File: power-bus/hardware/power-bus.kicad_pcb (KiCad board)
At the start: 2 copper layers, 109.2 x 68.6 mm, 18 parts, among them J1 CONN_01X02, J10 CONN_01X02, J11 CONN_01X02, J12 CONN_01X02, J13 CONN_01X02, J2 CONN_01X02, J3 CONN_01X02, J4 CONN_01X02, J5 CONN_01X02, J6 CONN_01X02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

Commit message: Mounting holes, logos.
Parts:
- added G***: LOGO, conservify:conservify_text_negative_4000, F.Cu at (188.3, 97.3)
- added M1: MOUNT_HOLE, conservify:HOLE_NPTH_3.2MM, F.Cu at (84.8, 52.1)
- added M2: MOUNT_HOLE, conservify:HOLE_NPTH_3.2MM, F.Cu at (169.8, 52.1)
- added M3: MOUNT_HOLE, conservify:HOLE_NPTH_3.2MM, F.Cu at (177.3, 115.1)
- moved J9 5.72 mm to (100.1, 52.1)
- moved J1 1.29 mm to (181.6, 54.5)
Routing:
- net /VADJ_1_EN: track 12.0 -> 16.0 mm
- net /12V0_2_EN: track 27.7 -> 29.5 mm
- net /12V0_1_EN: track 48.1 -> 49.8 mm
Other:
- board text added: "v0.1"

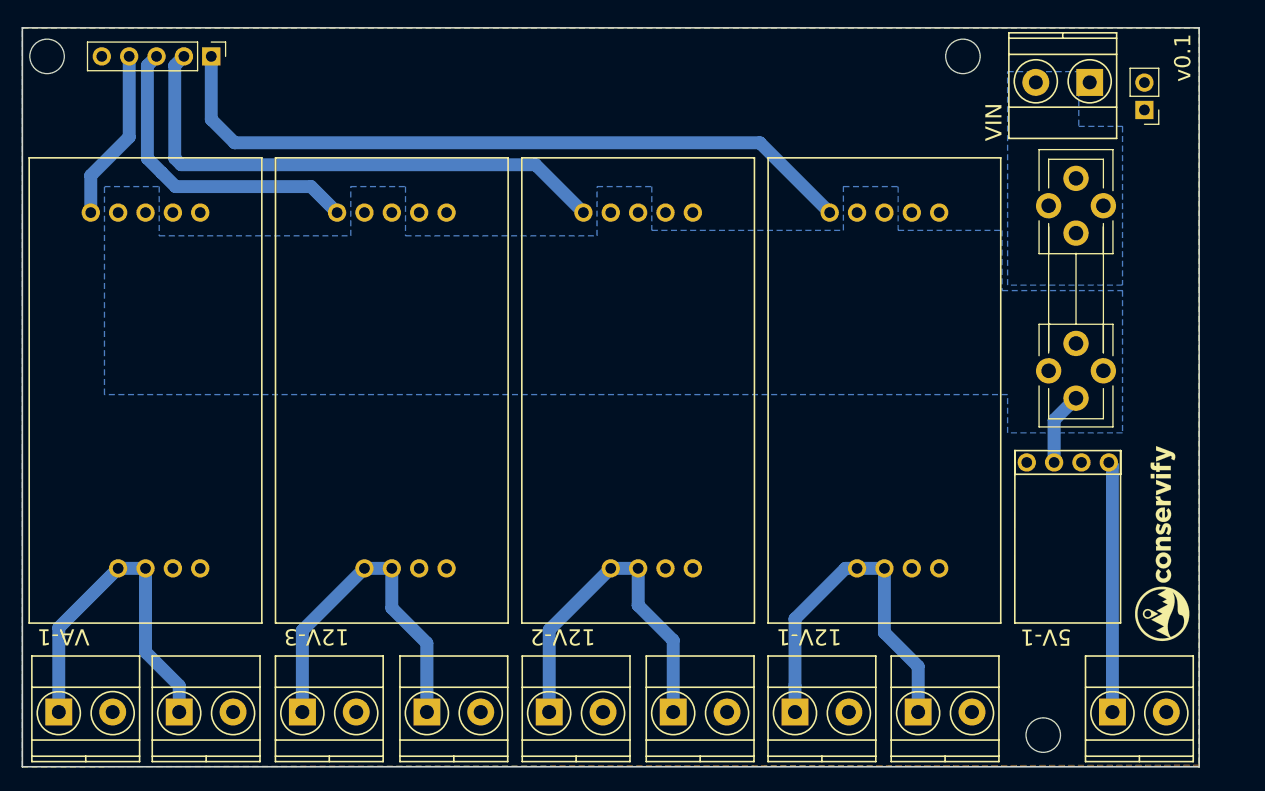
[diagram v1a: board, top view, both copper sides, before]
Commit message: Add better mounting holes, some labels, etc...
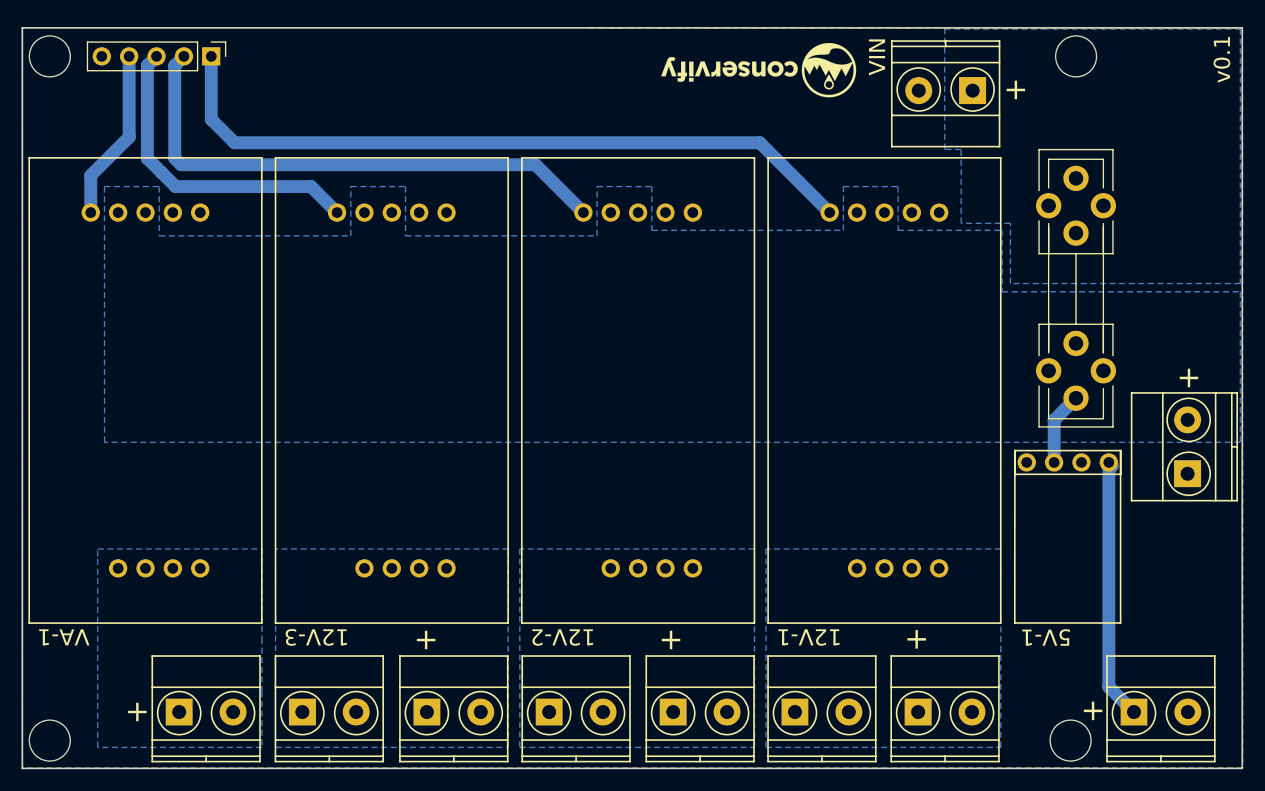
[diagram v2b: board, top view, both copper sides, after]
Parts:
- removed J12: CONN_01X02, Connectors_Terminal_Blocks:TerminalBlock_Pheonix_MKDS1.5-2pol
- removed J13: CONN_01X02, Socket_Strips:Socket_Strip_Straight_1x02_Pitch2.54mm
- added J8: CONN_01X02, Connectors_Terminal_Blocks:TerminalBlock_Pheonix_MKDS1.5-2pol, F.Cu at (190.7, 90.8)
- added M4: MOUNT_HOLE, conservify:HOLE_NPTH_3.8MM, F.Cu at (85.1, 115.6)
- M1, M2, M3: footprint conservify:HOLE_NPTH_3.2MM -> conservify:HOLE_NPTH_3.8MM
- moved G*** 57.7 mm to (150.9, 53.3), turned to 180 degrees
- moved J1 10.9 mm to (170.7, 55.2)
- moved M2 10.5 mm to (180.3, 52.1)
- moved M3 2.59 mm to (179.8, 115.6)
- moved J2 2.00 mm to (185.7, 112.9)
- moved M1 0.25 mm to (85.1, 52.1)
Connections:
- J1 pad 1: GND -> /VIN
- J1 pad 2: /VIN -> GND
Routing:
- net /12V0_3: track 33.5 -> 0.00 mm
- net /12V0_2: track 32.9 -> 0.00 mm
- net /12V0_1: track 32.9 -> 0.00 mm
- net /VADJ_1: track 32.8 -> 0.00 mm
- net /5V0_1: track 23.3 -> 24.6 mm
- added copper zone on B.Cu, net /12V0_1
- added copper zone on B.Cu, net /12V0_2
- added copper zone on B.Cu, net /12V0_3
- added copper zone on B.Cu, net /VADJ_1
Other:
- board size 109.2 x 68.6 mm -> 113.2 x 68.7 mm
- board text added: "+"

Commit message: Finishing touches on power bus board.
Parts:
- moved J2 1.82 mm to (187.5, 112.9)
- moved M3 0.83 mm to (180.6, 115.8)
- moved J9 0.38 mm to (100.1, 51.7)
- moved M2 0.36 mm to (180.6, 51.9)
- moved M1 0.20 mm to (85.1, 51.9)
- moved M4 0.20 mm to (85.1, 115.8)
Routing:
- net /12V0_3_EN: track 66.8 -> 71.2 mm
- net /5V0_1: track 24.6 -> 26.8 mm
- net /12V0_1_EN: track 49.8 -> 50.3 mm
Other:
- board text added: "12V1-EN"
- board text added: "12V2-EN"
- board text added: "12V3-EN"
- board text added: "VA-EN"

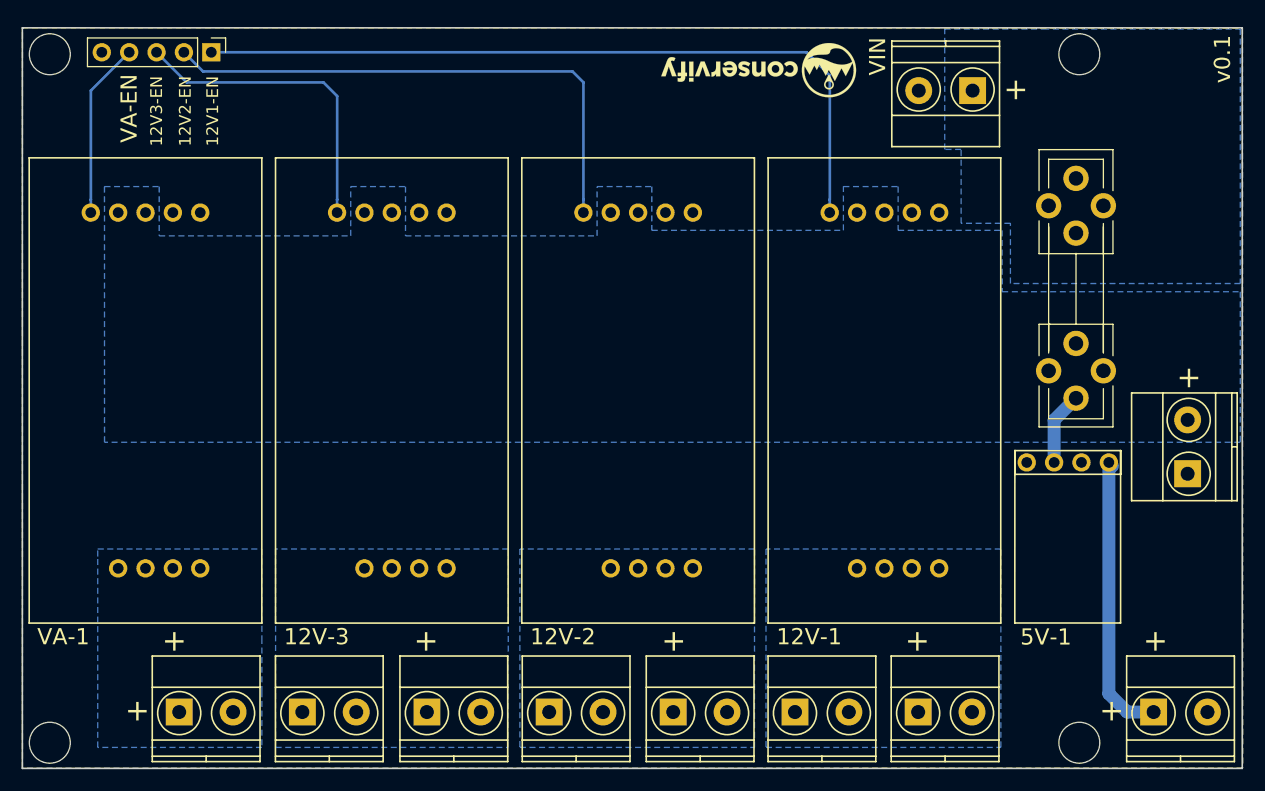
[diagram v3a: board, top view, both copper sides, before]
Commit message: Fix fuse footprint.
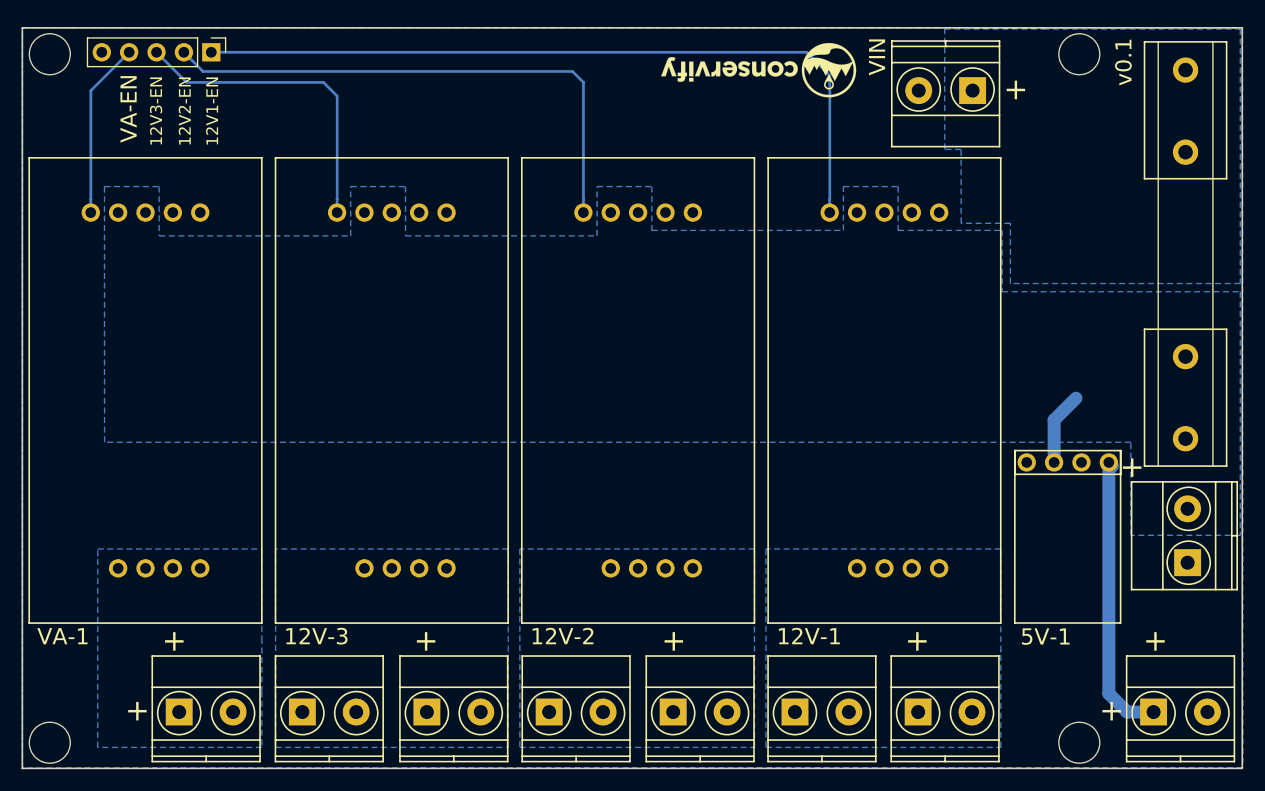
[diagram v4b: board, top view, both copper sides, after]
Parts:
- F1: footprint Fuse_Holders_and_Fuses:Fuseholder5x20_horiz_open_universal_Type-III -> conservify:Fuseholder6x30_horiz_open_inline_Type-I
- moved F1 10.8 mm to (190.5, 87.6)
- moved J8 8.25 mm to (190.7, 99.1)
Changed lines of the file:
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@@
 (kicad_pcb (version 4) (host pcbnew 4.0.6)
   (general
-    (links 60)
+    (links 56)
     (no_connects 0)
     (area 80.080476 46.655666 197.6655 119.89635)
@@
     (add_net GND)
   )
-  (module Fuse_Holders_and_Fuses:Fuseholder5x20_horiz_open_universal_Type-III (layer F.Cu)
-    (at 180.33226 83.79135 90)
-    (descr "Fuseholder, 5x20, open, horizontal, Type-III, universal, inline, lateral,")
-    (tags "Fuseholder 5x20 open horizontal Type-III universal inline lateral Sicherungshalter offen ")
-    (fp_text reference F1 (at 10.113 0 90) (layer F.SilkS) hide
-      (effects (font (size 1 1) (thickness 0.15)))
-    )
-    (fp_text value Fuse (at 12.74 6.35 90) (layer F.Fab) hide
-      (effects (font (size 1 1) (thickness 0.15)))
-    )
-    (fp_line (start 2.55 0) (end 17.9 0) (layer F.Fab) (width 0.1))
-    (fp_line (start -1.9 -2.55) (end 22.2 -2.55) (layer F.Fab) (width 0.1))
-    (fp_line (start 22.2 -2.55) (end 22.2 2.55) (layer F.Fab) (width 0.1))
-    (fp_line (start 22.2 2.55) (end -1.9 2.55) (layer F.Fab) (width 0.1))
-    (fp_line (start -1.9 2.55) (end -1.9 -2.5) (layer F.Fab) (width 0.1))
-    (fp_line (start 13.5 -3.35) (end 13.5 3.35) (layer F.Fab) (width 0.1))
-    (fp_line (start 13.5 3.35) (end 23.05 3.35) (layer F.Fab) (width 0.1))
-    (fp_line (start 23.05 3.35) (end 23.05 -3.3) (layer F.Fab) (width 0.1))
-    (fp_line (start 23.05 -3.3) (end 13.5 -3.35) (layer F.Fab) (width 0.1))
-    (fp_line (start -2.6 -3.35) (end 6.75 -3.35) (layer F.Fab) (width 0.1))
-    (fp_line (start 6.75 -3.35) (end 6.75 3.35) (layer F.Fab) (width 0.1))
-    (fp_line (start 6.75 3.35) (end -2.6 3.35) (layer F.Fab) (width 0.1))
-    (fp_line (start -2.6 3.35) (end -2.6 -3.35) (layer F.Fab) (width 0.1))
-    (fp_line (start 6.95 0) (end 13.45 0) (layer F.SilkS) (width 0.12))
-    (fp_line (start 6.86 3.43) (end 3.94 3.43) (layer F.SilkS) (width 0.12))
-    (fp_line (start -2.67 3.43) (end 1.14 3.43) (layer F.SilkS) (width 0.12))
-    (fp_line (start -1.9 2.54) (end 0.89 2.54) (layer F.SilkS) (width 0.12))
-    (fp_line (start 6.86 2.54) (end 4.19 2.54) (layer F.SilkS) (width 0.12))
-    (fp_line (start -2.67 -3.43) (end 1.14 -3.43) (layer F.SilkS) (width 0.12))
-    (fp_line (start -1.9 -2.54) (end 0.89 -2.54) (layer F.SilkS) (width 0.12))
-    (fp_line (start 6.86 -3.43) (end 3.94 -3.43) (layer F.SilkS) (width 0.12))
-    (fp_line (start 6.86 -2.54) (end 4.19 -2.54) (layer F.SilkS) (width 0.12))
-    (fp_line (start 13.41 -3.43) (end 16.46 -3.43) (layer F.SilkS) (width 0.12))
-    (fp_line (start 13.41 -2.54) (end 16.21 -2.54) (layer F.SilkS) (width 0.12))
-    (fp_line (start 13.41 2.54) (end 16.21 2.54) (layer F.SilkS) (width 0.12))
-    (fp_line (start 13.41 3.43) (end 16.46 3.43) (layer F.SilkS) (width 0.12))
-    (fp_line (start 23.07 3.43) (end 19.26 3.43) (layer F.SilkS) (width 0.12))
-    (fp_line (start 22.18 2.54) (end 19.51 2.54) (layer F.SilkS) (width 0.12))
-    (fp_line (start 23.07 -3.43) (end 19.26 -3.43) (layer F.SilkS) (width 0.12))
-    (fp_line (start 22.18 -2.54) (end 19.51 -2.54) (layer F.SilkS) (width 0.12))
-    (fp_line (start 23.07 -3.43) (end 23.07 3.43) (layer F.SilkS) (width 0.12))
-    (fp_line (start 13.41 3.43) (end 13.41 2.54) (layer F.SilkS) (width 0.12))
-    (fp_line (start 13.41 -3.43) (end 13.41 -2.54) (layer F.SilkS) (width 0.12))
-    (fp_line (start -2.67 -3.43) (end -2.67 3.43) (layer F.SilkS) (width 0.12))
-    (fp_line (start 6.86 3.43) (end 6.86 2.54) (layer F.SilkS) (width 0.12))
-    (fp_line (start 6.86 -3.43) (end 6.86 -2.41) (layer F.SilkS) (width 0.12))
-    (fp_line (start 15.91 2.54) (end 4.23 2.54) (layer F.SilkS) (width 0.12))
-    (fp_line (start 4.36 -2.54) (end 15.91 -2.54) (layer F.SilkS) (width 0.12))
-    (fp_line (start 6.86 0) (end 6.86 -2.54) (layer F.SilkS) (width 0.12))
-    (fp_line (start -1.91 -2.54) (end -1.91 2.54) (layer F.SilkS) (width 0.12))
-    (fp_line (start 6.86 2.54) (end 6.86 0) (layer F.SilkS) (width 0.12))
-    (fp_line (start 13.41 0) (end 13.41 -2.54) (layer F.SilkS) (width 0.12))
-    (fp_line (start 22.17 -2.54) (end 22.17 2.54) (layer F.SilkS) (width 0.12))
-    (fp_line (start 13.41 2.54) (end 13.41 0) (layer F.SilkS) (width 0.12))
-    (fp_line (start -2.85 -3.96) (end 23.3 -3.96) (layer F.CrtYd) (width 0.05))
-    (fp_line (start -2.85 -3.96) (end -2.85 3.96) (layer F.CrtYd) (width 0.05))
-    (fp_line (start 23.3 3.96) (end 23.3 -3.96) (layer F.CrtYd) (width 0.05))
-    (fp_line (start 23.3 3.96) (end -2.85 3.96) (layer F.CrtYd) (width 0.05))
-    (pad 2 thru_hole circle (at 15.32 0 90) (size 2.35 2.35) (drill 1.35) (layers *.Cu *.Mask)
-      (net 13 /VIN))
-    (pad 2 thru_hole circle (at 20.4 0 90) (size 2.35 2.35) (drill 1.35) (layers *.Cu *.Mask)
-      (net 13 /VIN))
-    (pad 1 thru_hole circle (at 5.08 0 90) (size 2.35 2.35) (drill 1.35) (layers *.Cu *.Mask)
-      (net 2 /VRAW))
-    (pad 1 thru_hole circle (at 0 0 90) (size 2.35 2.35) (drill 1.35) (layers *.Cu *.Mask)
-      (net 2 /VRAW))
-    (pad 2 thru_hole circle (at 17.86 -2.54 90) (size 2.35 2.35) (drill 1.35) (layers *.Cu *.Mask)
-      (net 13 /VIN))
-    (pad 2 thru_hole circle (at 17.86 2.54 90) (size 2.35 2.35) (drill 1.35) (layers *.Cu *.Mask)
-      (net 13 /VIN))
-    (pad 1 thru_hole circle (at 2.54 -2.54 90) (size 2.35 2.35) (drill 1.35) (layers *.Cu *.Mask)
-      (net 2 /VRAW))
-    (pad 1 thru_hole circle (at 2.54 2.54 90) (size 2.35 2.35) (drill 1.35) (layers *.Cu *.Mask)
-      (net 2 /VRAW))
-  )
   (module conservify:pololu-vreg (layer F.Cu)
     (at 179.57026 89.75655 180)
@@
   )
   (module Connectors_Terminal_Blocks:TerminalBlock_Pheonix_MKDS1.5-2pol (layer F.Cu)
-    (at 190.6905 90.805 90)
+    (at 190.6905 99.06 90)
     (descr "2-way 5mm pitch terminal block, Phoenix MKDS series")
     (fp_text reference J8 (at 2.5 5.9 90) (layer F.SilkS) hide
@@
       (xy -6.476371 -1.79874)) (layer F.SilkS) (width 0.01))
   )
+  (module conservify:Fuseholder6x30_horiz_open_inline_Type-I (layer F.Cu)
+    (at 190.5 87.5538 90)
+    (descr "Fuseholder, 5x20, open, horizontal, Type-I, Inline,")
+    (tags "Fuseholder 5x20 open horizontal Type-I Inline Sicherungshalter offen ")
+    (fp_text reference F1 (at 17.78 -5.08 90) (layer F.SilkS) hide
+      (effects (font (size 1 1) (thickness 0.15)))
+    )
+    (fp_text value Fuse (at 17.5768 0 90) (layer F.Fab) hide
+      (effects (font (size 1 1) (thickness 0.15)))
+    )
+    (fp_line (start 36.83 3.81) (end 36.83 -3.81) (layer F.SilkS) (width 0.15))
+    (fp_line (start 24.13 3.81) (end 36.83 3.81) (layer F.SilkS) (width 0.15))
+    (fp_line (start 24.13 -3.81) (end 24.13 3.81) (layer F.SilkS) (width 0.15))
+    (fp_line (start 10.16 3.81) (end 10.16 -3.81) (layer F.SilkS) (width 0.15))
+    (fp_line (start -2.54 3.81) (end 10.16 3.81) (layer F.SilkS) (width 0.15))
+    (fp_line (start -2.54 -3.81) (end -2.54 3.81) (layer F.SilkS) (width 0.15))
+    (fp_line (start 24.13 3.81) (end 36.83 3.81) (layer F.SilkS) (width 0.15))
+    (fp_line (start 36.83 -2.54) (end -2.54 -2.54) (layer F.SilkS) (width 0.12))
+    (fp_line (start 36.83 2.54) (end -2.54 2.54) (layer F.SilkS) (width 0.12))
+    (fp_line (start 24.13 -3.81) (end 36.83 -3.81) (layer F.SilkS) (width 0.15))
+    (fp_line (start -2.54 -3.81) (end 10.16 -3.81) (layer F.SilkS) (width 0.15))
+    (fp_line (start -2.54 3.81) (end 10.16 3.81) (layer F.SilkS) (width 0.15))
+    (pad 2 thru_hole circle (at 26.5938 0 90) (size 2.35 2.35) (drill 1.35) (layers *.Cu *.Mask)
+      (net 13 /VIN))
+    (pad 2 thru_hole circle (at 34.2138 0 90) (size 2.35 2.35) (drill 1.35) (layers *.Cu *.Mask)
+      (net 13 /VIN))
+    (pad 1 thru_hole circle (at 7.62 0 90) (size 2.35 2.35) (drill 1.35) (layers *.Cu *.Mask)
+      (net 2 /VRAW))
+    (pad 1 thru_hole circle (at 0 0 90) (size 2.35 2.35) (drill 1.35) (layers *.Cu *.Mask)
+      (net 2 /VRAW))
+  )
   (gr_text 12V1-EN (at 100.203 57.15 90) (layer F.SilkS)
     (effects (font (size 1.1 1.1) (thickness 0.2)))
@@
   (gr_line (start 85.09 52.07) (end 85.09 115.57) (layer F.Fab) (width 0.2))
   (gr_line (start 85.09 52.07) (end 180.34 52.07) (layer F.Fab) (width 0.2))
-  (gr_text + (at 190.8175 81.8515) (layer F.SilkS)
+  (gr_text + (at 185.547 90.17) (layer F.SilkS)
     (effects (font (size 2 2) (thickness 0.3)) (justify mirror))
   )
@@
     (effects (font (size 2 2) (thickness 0.3)) (justify mirror))
   )
-  (gr_text v0.1 (at 193.929 52.324 90) (layer F.SilkS)
+  (gr_text v0.1 (at 184.785 52.578 90) (layer F.SilkS)
     (effects (font (size 1.5 1.5) (thickness 0.3)))
   )
@@
     (polygon
       (pts
-        (xy 195.58 73.914) (xy 195.58 87.884) (xy 174.244 87.884) (xy 90.17 87.884) (xy 90.16226 64.15335)
-        (xy 95.24226 64.15335) (xy 95.24226 68.72535) (xy 113.02226 68.72535) (xy 113.02226 64.15335) (xy 118.10226 64.15335)
-        (xy 118.10226 68.72535) (xy 135.88226 68.72535) (xy 135.88226 64.15335) (xy 140.96226 64.15335) (xy 140.96226 68.21735)
-        (xy 158.74226 68.21735) (xy 158.74226 64.15335) (xy 163.82226 64.15335) (xy 163.82226 68.21735) (xy 173.47426 68.21735)
-        (xy 173.482 73.914)
+        (xy 95.24226 68.72535) (xy 113.02226 68.72535) (xy 113.02226 64.15335) (xy 118.10226 64.15335) (xy 118.10226 68.72535)
+        (xy 135.88226 68.72535) (xy 135.88226 64.15335) (xy 140.96226 64.15335) (xy 140.96226 68.21735) (xy 158.74226 68.21735)
+        (xy 158.74226 64.15335) (xy 163.82226 64.15335) (xy 163.82226 68.21735) (xy 173.47426 68.21735) (xy 173.482 73.914)
+        (xy 195.58 73.914) (xy 195.58 96.52) (xy 185.42 96.52) (xy 185.42 87.884) (xy 90.17 87.884)
+        (xy 90.16226 64.15335) (xy 95.24226 64.15335)
       )
     )
